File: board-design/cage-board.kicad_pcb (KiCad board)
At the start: 2 copper layers, 160 x 160 mm, 58 parts, among them J1 Jack-DC, J10 73131-0240, J11 73131-0240, J12 73131-0240, J13 Conn_01x02, J14 Conn_01x02, J15 Conn_02x13_test_points, J16 TB002-500-03BE, J17 TB002-500-03BE, J18 TB002-500-03BE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

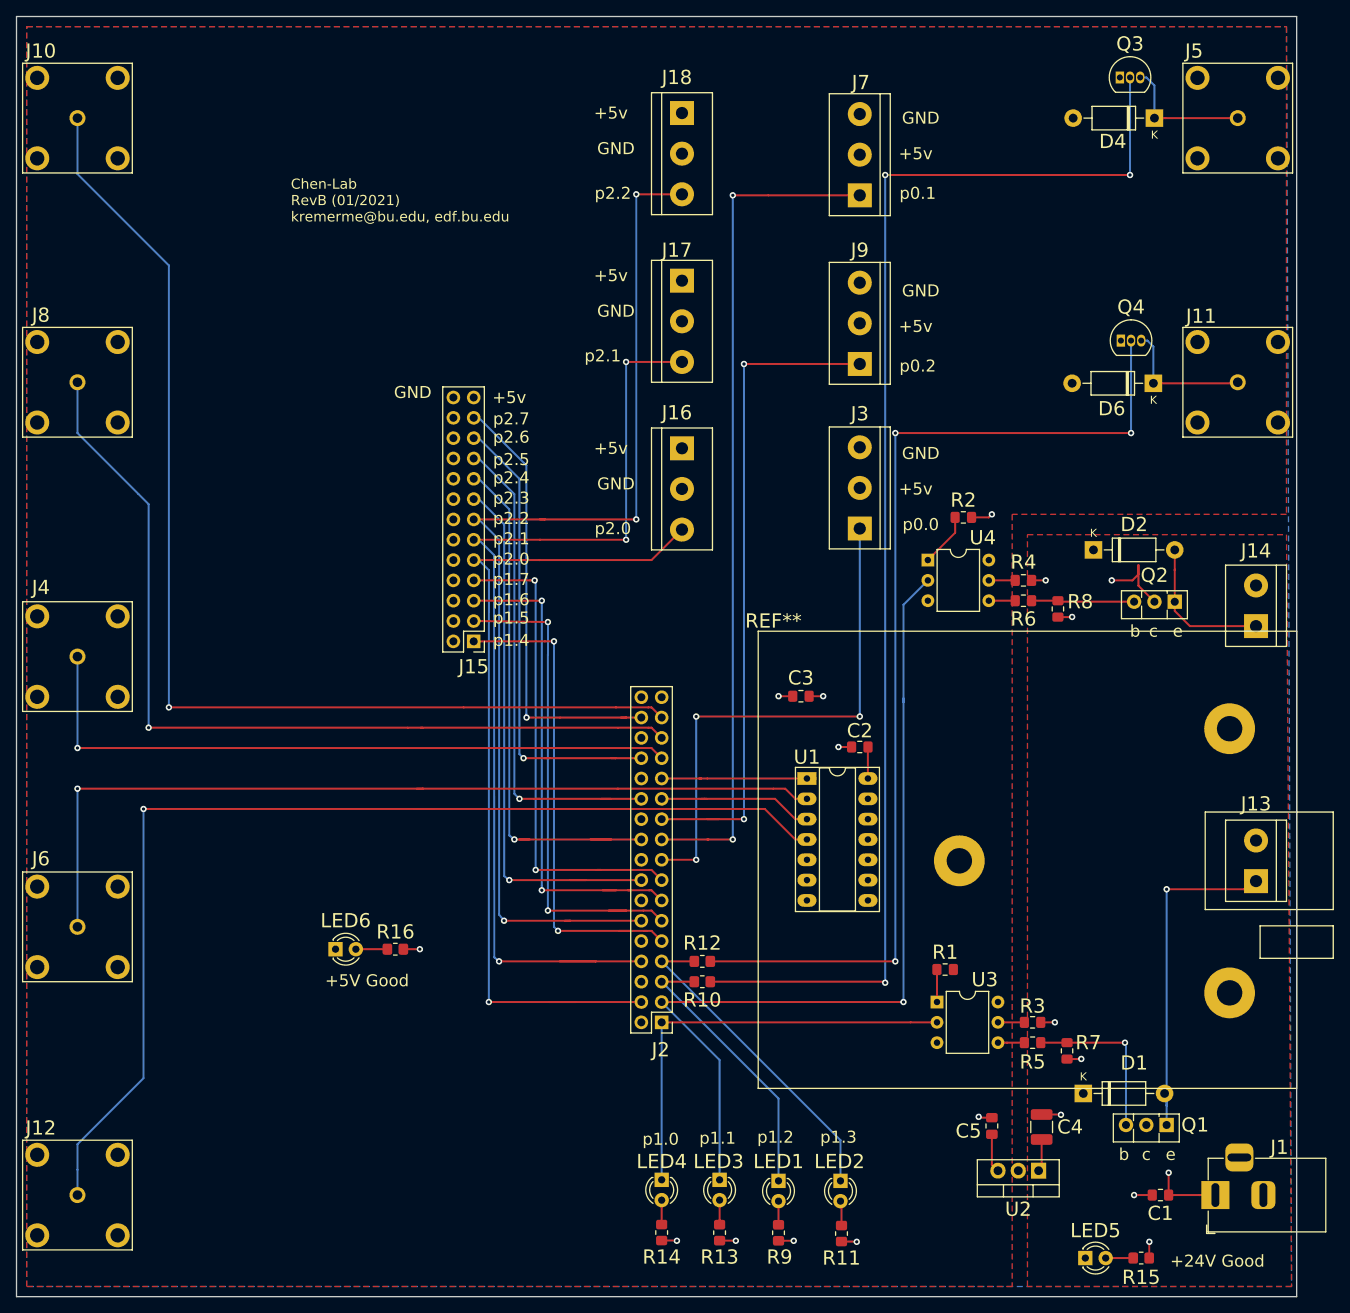
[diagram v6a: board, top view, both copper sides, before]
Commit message: changin to right angle LEDs, fixing terminal blocks, fixing DC-DC footprint
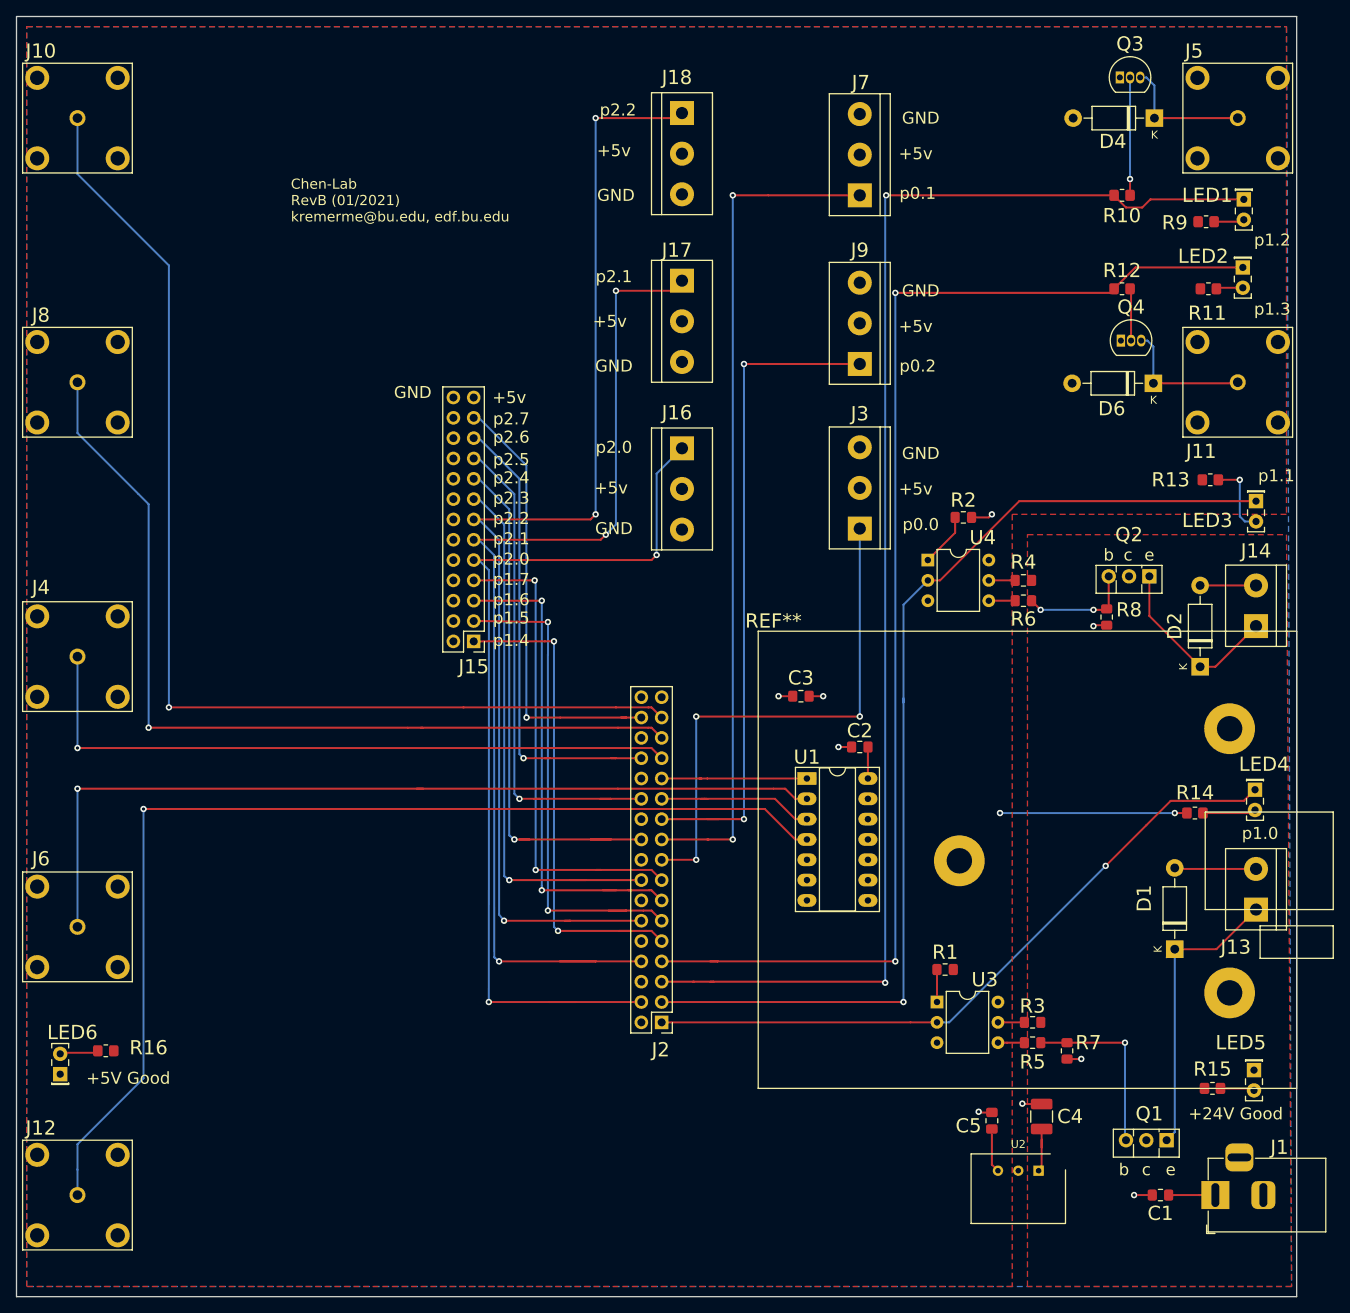
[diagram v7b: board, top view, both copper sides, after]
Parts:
- LED1, LED2, LED3, LED4, LED5, LED6: footprint LED_THT:LED_D3.0mm -> LED_THT:LED_Rectangular_W5.0mm_H2.0mm
- U2: footprint Package_TO_SOT_THT:TO-220-3_Vertical -> Package_SIP:SIP3_11.6x8.5mm
- moved R9 137.2 mm to (191.9, 25.7), turned to 0 degrees
- moved LED1 135.8 mm to (196.6, 22.9)
- moved R11 126.7 mm to (192.2, 34.0), turned to 0 degrees
- moved LED2 124.8 mm to (196.5, 31.4)
- moved R13 112.3 mm to (192.4, 57.9), turned to 0 degrees
- moved R10 111.4 mm to (181.4, 22.4)
- moved LED3 108.1 mm to (198.1, 60.6)
- moved R12 99.1 mm to (181.4, 34.0)
- moved LED4 88.8 mm to (198.0, 96.6)
- moved R14 84.8 mm to (190.5, 99.6), turned to 0 degrees
- moved R16 38.4 mm to (54.3, 129.3)
- moved LED6 37.8 mm to (48.6, 132.2), turned to 90 degrees
- moved LED5 31.6 mm to (197.9, 131.7), turned to 270 degrees
- moved R15 23.0 mm to (192.7, 134.0), turned to 0 degrees
- moved D1 21.4 mm to (188.0, 116.6), turned to 90 degrees
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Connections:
- D1 pad 1: +24V -> Net-(D1-Pad1)
- D1 pad 2: Net-(D1-Pad2) -> GND
- D2 pad 1: +24V -> Net-(D2-Pad1)
- D2 pad 2: Net-(D2-Pad2) -> GND
- J13 pad 1: Net-(D1-Pad2) -> Net-(D1-Pad1)
- J14 pad 1: Net-(D2-Pad2) -> Net-(D2-Pad1)
- J16 pad 1: +5V -> /P2.0
- J16 pad 2: GND -> +5V
- J16 pad 3: /P2.0 -> GND
- J17 pad 1: +5V -> /P2.1
- J17 pad 2: GND -> +5V
- J17 pad 3: /P2.1 -> GND
- J18 pad 1: +5V -> /P2.2
- J18 pad 2: GND -> +5V
- J18 pad 3: /P2.2 -> GND
- Q1 pad 1: Net-(D1-Pad2) -> Net-(D1-Pad1)
- Q2 pad 1: Net-(D2-Pad2) -> Net-(D2-Pad1)
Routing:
- net Net-(Q3-Pad2): track 166.3 -> 14.7 mm, vias 3 -> 1
- net /P1.2: track 35.0 -> 172.9 mm, vias 0 -> 2
- net Net-(Q4-Pad2): track 130.8 -> 6.53 mm, vias 3 -> 0
- net /P1.3: track 40.8 -> 158.4 mm, vias 0 -> 2
- net Net-(D1-Pad2): track 45.3 -> 0.00 mm, vias 1 -> 0
- net Net-(D1-Pad1): track 0.00 -> 37.9 mm
- net /P1.0: track 54.1 -> 86.6 mm, vias 0 -> 1
- net Net-(D2-Pad1): track 0.00 -> 23.0 mm
- net /P1.1: track 109.9 -> 129.8 mm
- net Net-(D2-Pad2): track 18.7 -> 0.00 mm
- net GND: track 14.0 -> 31.1 mm
- net +24V: track 28.4 -> 12.2 mm, vias 5 -> 0
- net +5V: track 23.1 -> 36.6 mm, vias 7 -> 4
- net /P2.0: track 105.6 -> 115.8 mm, vias 1 -> 2
- net /P2.2: track 136.6 -> 145.3 mm
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
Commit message: fixing 5v led
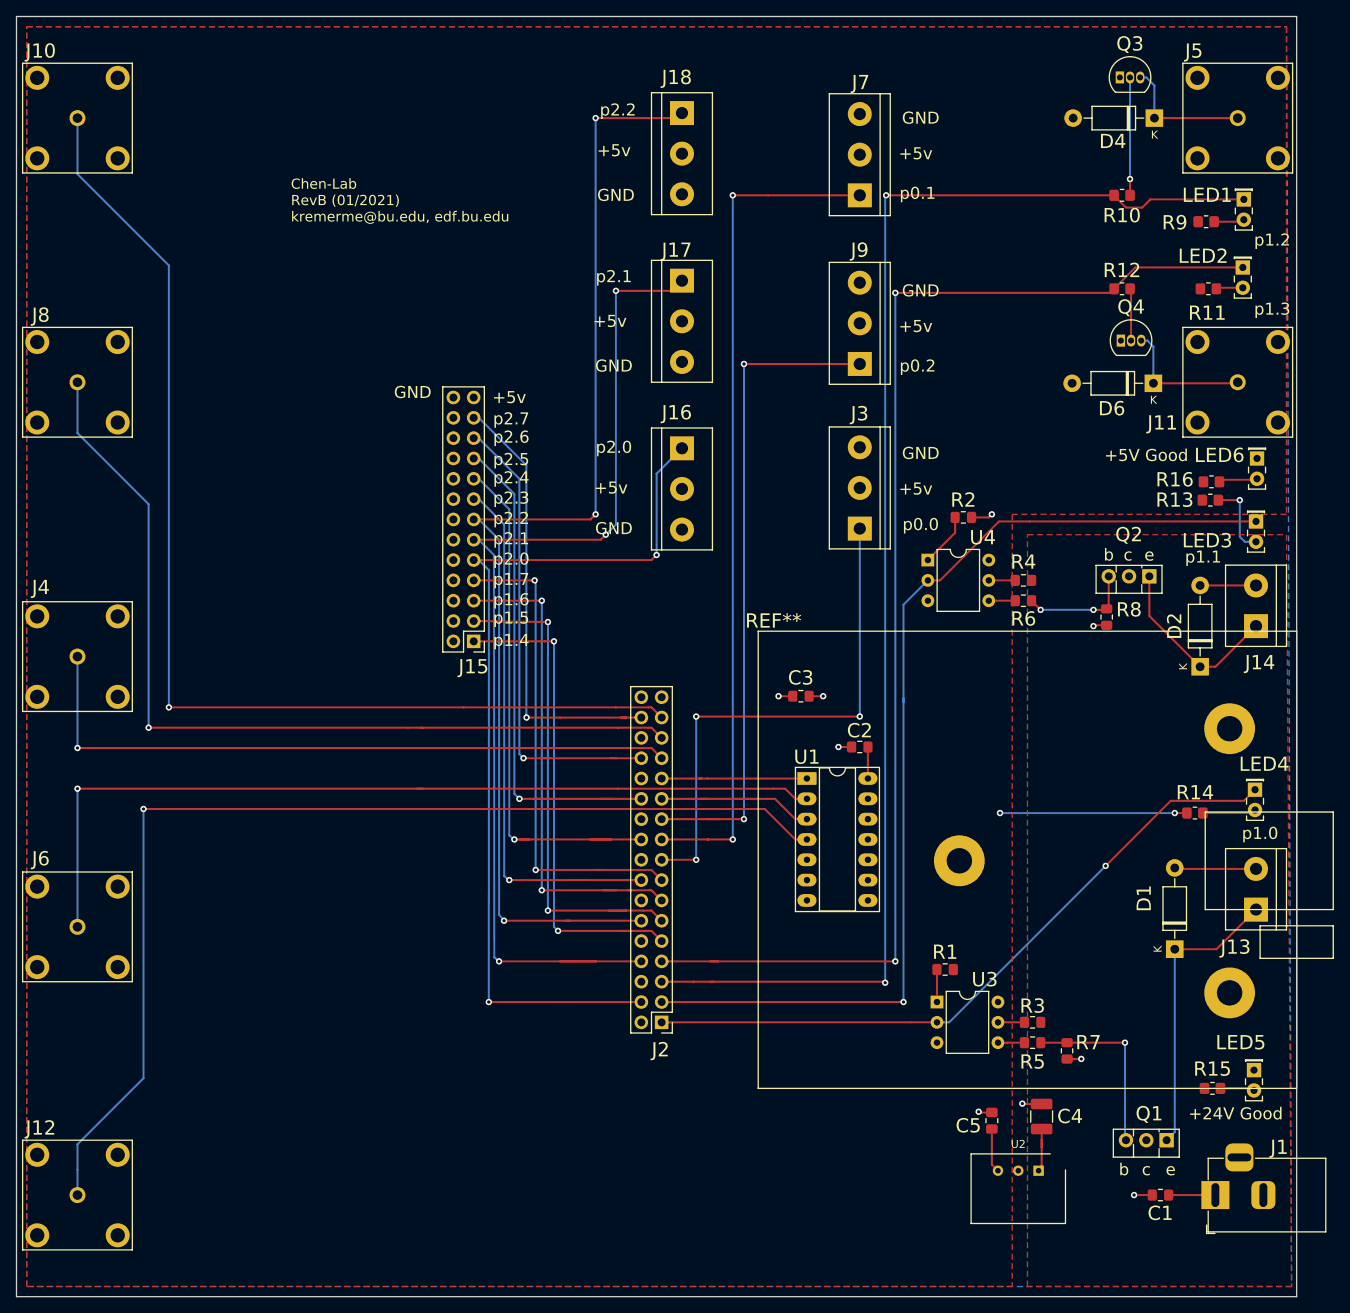
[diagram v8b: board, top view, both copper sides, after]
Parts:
- moved LED6 168.2 mm to (198.2, 55.2), turned to 270 degrees
- moved R16 155.4 mm to (192.5, 58.2), turned to 0 degrees
- moved LED3 2.54 mm to (198.1, 63.1)
- moved R13 2.54 mm to (192.4, 60.5)
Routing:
- net /P1.1: track 129.8 -> 128.8 mm
